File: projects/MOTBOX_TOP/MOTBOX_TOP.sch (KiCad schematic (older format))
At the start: 6 parts, among them J10 JST_Female_4pin, J11 JST_Female_4pin, J12 JST_Female_2pin, J13 JST_Female_2pin, J9 JST_Female_2pin, M1 Motor

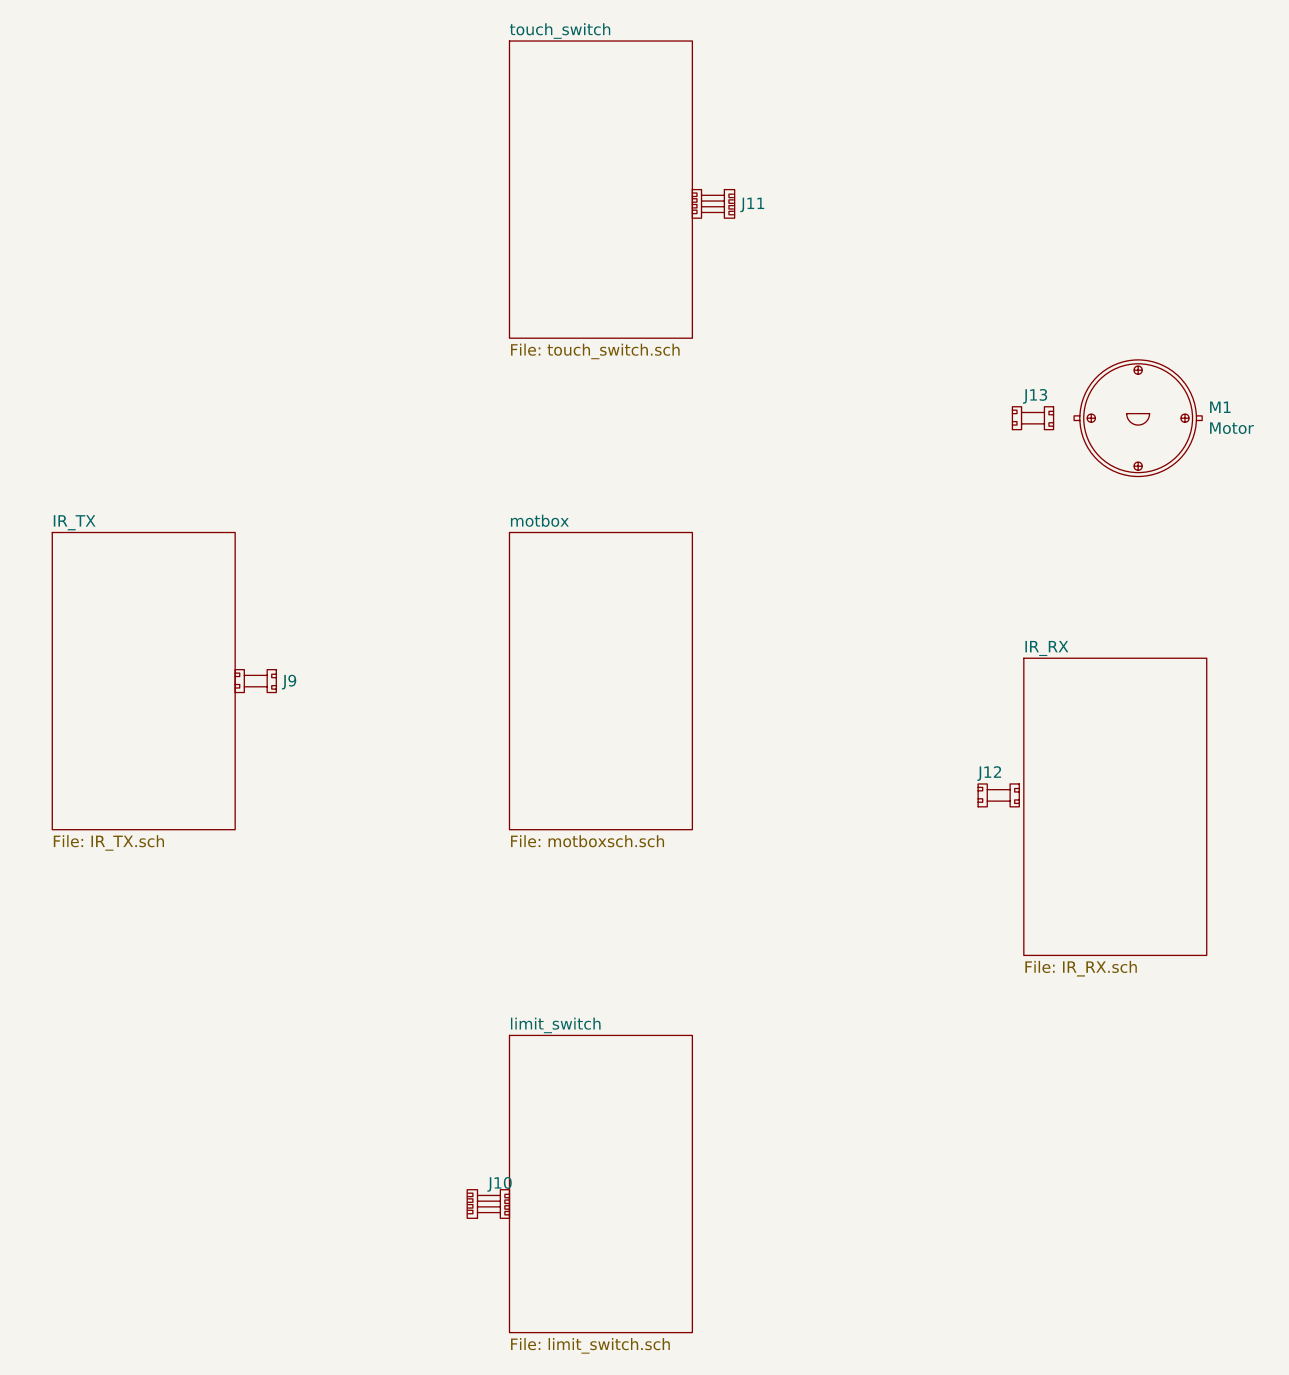
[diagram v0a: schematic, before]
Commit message: Changes for the motbox with promini instead of nano
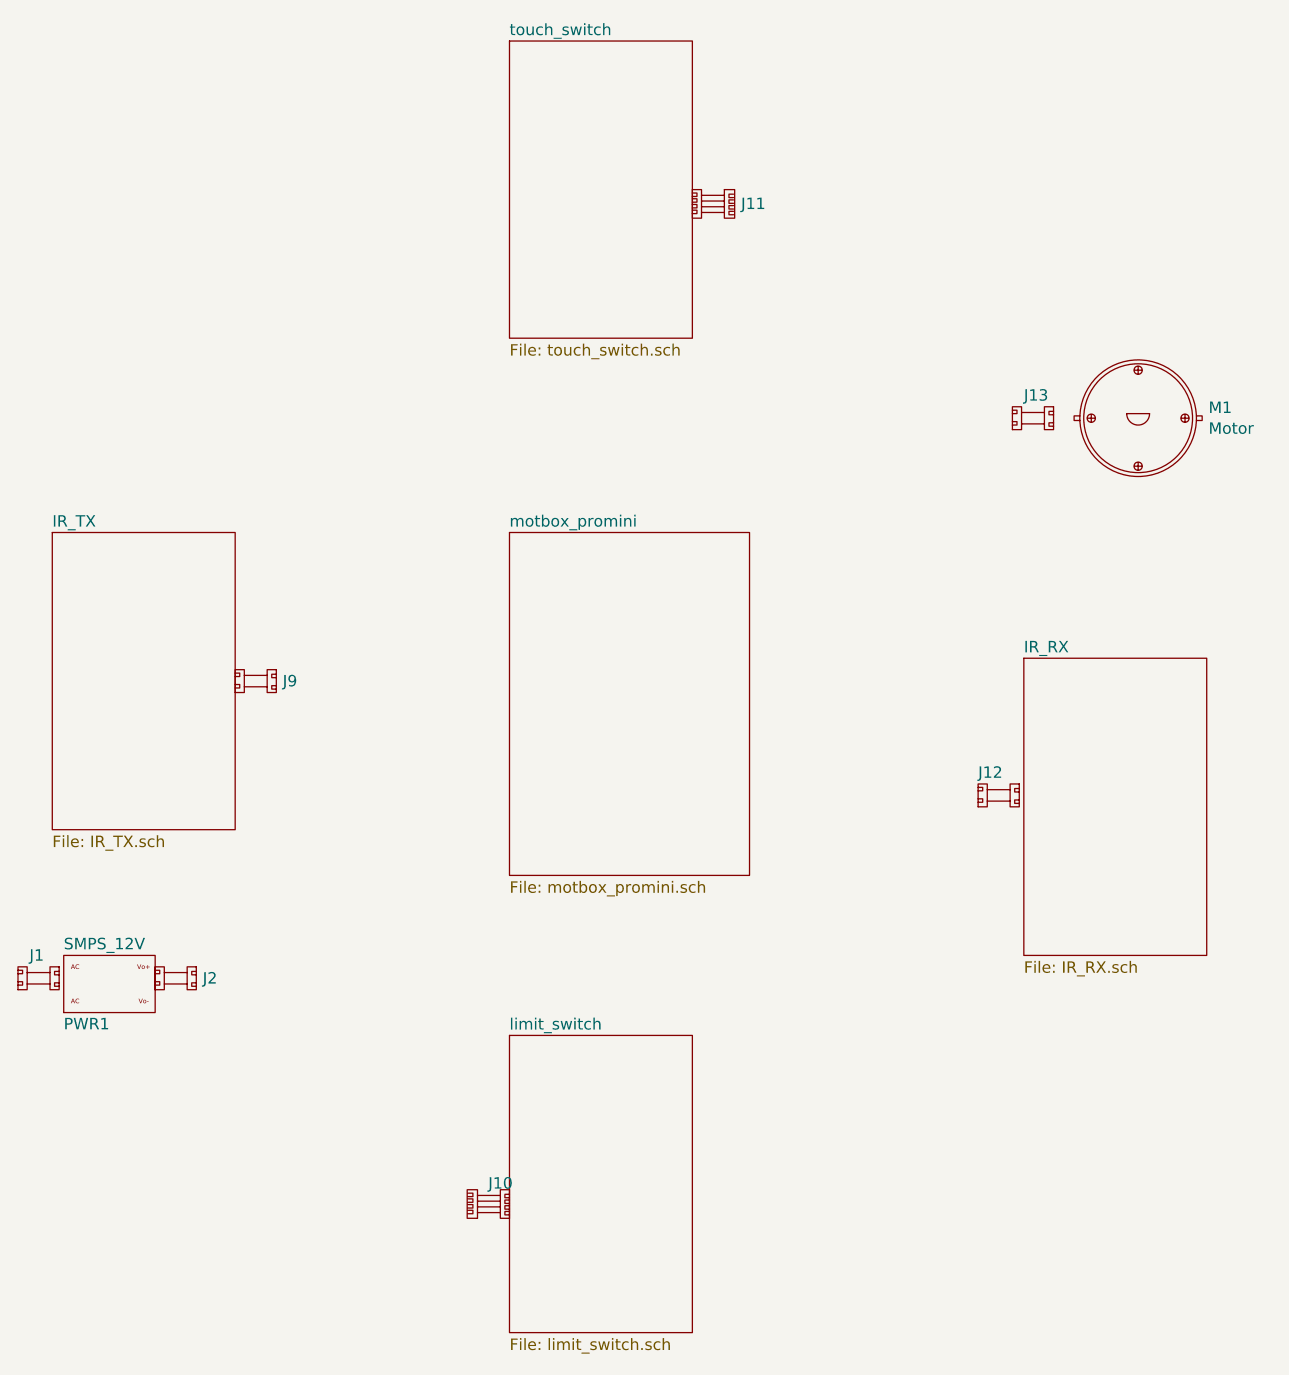
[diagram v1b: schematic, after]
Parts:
- added J1, J2: JST_Female_2pin, symbol hitesh_custom:JST_Female_2pin
- added PWR1: SMPS_12V, symbol hitesh_custom:SMPS
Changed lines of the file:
@@
 EESchema Schematic File Version 4
-LIBS:motbox-cache
-LIBS:ir_tx_led-cache
-LIBS:ir_rx_led-cache
-LIBS:touch_switch-cache
-LIBS:limit_switch-cache
+LIBS:MOTBOX_TOP-cache
+LIBS:motbox_with_promini-cache
 EELAYER 26 0
 EELAYER END
@@
 Comment4 ""
 $EndDescr
-$Sheet
-S 4850 3250 800  1300
-U 5CC074B5
-F0 "motbox" 50
-F1 "motboxsch.sch" 50
-$EndSheet
 $Sheet
 S 2850 3250 800  1300
@@
 F 1 "JST_Female_2pin" H 3858 3955 50  0001 L CNN
 F 2 "" H 3650 3950 50  0001 C CNN
-F 3 "" H 3650 3950 50  0001 C CNN
+F 3 "" H 3650 3950 50  0000 C CNN
 	1    3650 3950
 	1    0    0    -1
@@
 F 1 "JST_Female_4pin" H 5863 2043 50  0001 L CNN
 F 2 "" H 5700 2200 50  0001 C CNN
-F 3 "" H 5700 2200 50  0001 C CNN
+F 3 "" H 5700 2200 50  0000 C CNN
 	1    6000 1950
 	1    0    0    -1
@@
 	1    0    0    -1
 $EndComp
+$Comp
+L hitesh_custom:SMPS PWR1
+U 1 1 5CC91415
+P 2900 5350
+F 0 "PWR1" H 2900 5300 50  0000 L CNN
+F 1 "SMPS_12V" H 2900 5650 50  0000 L CNN
+F 2 "" H 2900 5350 50  0001 C CNN
+F 3 "" H 2900 5350 50  0001 C CNN
+	1    2900 5350
+	1    0    0    -1
+$EndComp
+$Comp
+L hitesh_custom:JST_Female_2pin J1
+U 1 1 5CC919BD
+P 2700 5250
+F 0 "J1" H 2750 5400 50  0000 L CNN
+F 1 "JST_Female_2pin" H 2908 5255 50  0001 L CNN
+F 2 "" H 2700 5250 50  0001 C CNN
+F 3 "" H 2700 5250 50  0001 C CNN
+	1    2700 5250
+	1    0    0    -1
+$EndComp
+$Comp
+L hitesh_custom:JST_Female_2pin J2
+U 1 1 5CC91AE0
+P 3300 5250
+F 0 "J2" H 3508 5300 50  0000 L CNN
+F 1 "JST_Female_2pin" H 3508 5255 50  0001 L CNN
+F 2 "" H 3300 5250 50  0001 C CNN
+F 3 "" H 3300 5250 50  0001 C CNN
+	1    3300 5250
+	1    0    0    -1
+$EndComp
+$Sheet
+S 4850 3250 1050 1500
+U 5CCC7C1B
+F0 "motbox_promini" 50
+F1 "motbox_promini.sch" 50
+$EndSheet
 $EndSCHEMATC
